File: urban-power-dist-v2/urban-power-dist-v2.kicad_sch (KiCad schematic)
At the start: 4 parts, among them J1 12V_IN

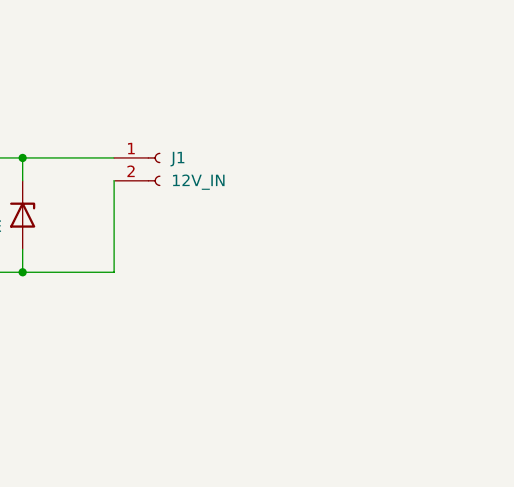
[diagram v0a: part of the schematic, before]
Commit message: update tvs diode, layout changes
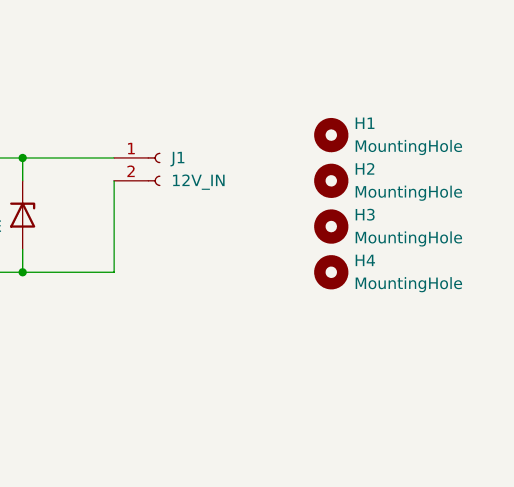
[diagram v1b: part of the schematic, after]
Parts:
- added H1, H2, H3, H4: MountingHole, MountingHole:MountingHole_3.2mm_M3, symbol Mechanical:MountingHole
- D1: footprint Diode_SMD:Nexperia_DSN1608-2_1.6x0.8mm -> Diode_SMD:D_SMF

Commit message: layout DRC fixes
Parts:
- J1: footprint ATF13-2P-BM03:ATF132PBM03 -> connector footprint:ATF132PBM03
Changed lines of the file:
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@@
 			)
 		)
-		(property "Footprint" "ATF13-2P-BM03:ATF132PBM03"
+		(property "Footprint" "connector footprint:ATF132PBM03"
 			(at 184.15 40.64 0)
 			(effects
